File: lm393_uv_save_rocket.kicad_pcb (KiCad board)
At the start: 2 copper layers, 35 x 74 mm, 14 parts, among them J1 BAT 9V, J2 IGNITER, M3 M3, Q1 TIP122, U1 LM7805, U2 LM393

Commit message: Ajuste trilhas placa
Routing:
- net Net-(J2-Pin_1): track 35.3 -> 29.6 mm
- net Net-(D2-K): track 28.9 -> 34.1 mm
- net Net-(D2-A): track 27.0 -> 27.7 mm
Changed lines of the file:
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@@
+	)
+	(segment
+		(start 109 115.5)
+		(end 109 120.54)
+		(width 1.25)
+		(layer "B.Cu")
+		(net 2)
+	)
+	(segment
+		(start 110.747256 113.752744)
+		(end 109 115.5)
+		(width 1.25)
+		(layer "B.Cu")
+		(net 2)
 	)
 	(segment
@@
 	)
 	(segment
+		(start 109 120.54)
+		(end 110.75 120.54)
+		(width 1.25)
+		(layer "B.Cu")
+		(net 2)
+	)
+	(segment
 		(start 105.25 120.54)
-		(end 110.75 120.54)
+		(end 109 120.54)
 		(width 1.25)
 		(layer "B.Cu")
@@
 	(segment
 		(start 110.747256 109.77)
-		(end 110.747256 120.537256)
+		(end 110.747256 113.752744)
 		(width 1.25)
 		(layer "B.Cu")
@@
 	)
 	(segment
-		(start 108.705 128.25)
-		(end 105.25 128.25)
-		(width 1.25)
-		(layer "B.Cu")
-		(net 3)
-	)
-	(segment
-		(start 101.5 124.5)
-		(end 101.5 113.75)
+		(start 98.25 122.5)
+		(end 98.25 114)
 		(width 1.25)
 		(layer "B.Cu")
@@
 	)
 	(segment
+		(start 108.207256 111.457256)
+		(end 108.207256 109.77)
+		(width 1.25)
+		(layer "B.Cu")
+		(net 3)
+	)
+	(segment
+		(start 104 128.25)
+		(end 98.25 122.5)
+		(width 1.25)
+		(layer "B.Cu")
+		(net 3)
+	)
+	(segment
+		(start 108.705 128.25)
+		(end 104 128.25)
+		(width 1.25)
+		(layer "B.Cu")
+		(net 3)
+	)
+	(segment
+		(start 99.5 112.75)
+		(end 107 112.75)
+		(width 1.25)
+		(layer "B.Cu")
+		(net 3)
+	)
+	(segment
+		(start 98.25 114)
+		(end 99.5 112.75)
+		(width 1.25)
+		(layer "B.Cu")
+		(net 3)
+	)
+	(segment
 		(start 107 112.75)
 		(end 108.25 111.5)
@@
 	)
 	(segment
-		(start 105.25 128.25)
-		(end 101.5 124.5)
-		(width 1.25)
-		(layer "B.Cu")
-		(net 3)
-	)
-	(segment
-		(start 102.5 112.75)
-		(end 107 112.75)
-		(width 1.25)
-		(layer "B.Cu")
-		(net 3)
-	)
-	(segment
-		(start 108.207256 111.457256)
-		(end 108.207256 109.77)
-		(width 1.25)
-		(layer "B.Cu")
-		(net 3)
-	)
-	(segment
-		(start 101.5 113.75)
-		(end 102.5 112.75)
-		(width 1.25)
-		(layer "B.Cu")
-		(net 3)
-	)
-	(segment
 		(start 110.1637 95.5274)
 		(end 106.9137 95.5274)
@@
 	)
 	(segment
-		(start 89.75 128.25)
-		(end 89.75 126.25)
+		(start 89.529 98.856)
+		(end 89.529 128.044)
 		(width 1.25)
 		(layer "B.Cu")
@@
 	)
 	(segment
-		(start 96.75 119.25)
-		(end 96.75 108.5)
+		(start 89.615 98.77)
+		(end 89.529 98.856)
 		(width 1.25)
 		(layer "B.Cu")
@@
 	)
 	(segment
-		(start 89.75 126.25)
-		(end 96.75 119.25)
-		(width 1.25)
-		(layer "B.Cu")
-		(net 5)
-	)
-	(segment
-		(start 96.75 108.5)
-		(end 89.615 101.365)
-		(width 1.25)
-		(layer "B.Cu")
-		(net 5)
-	)
-	(segment
-		(start 89.615 101.365)
-		(end 89.615 98.77)
-		(width 1.25)
-		(layer "B.Cu")
+		(start 89.529 128.044)
+		(end 89.735 128.25)
+		(width 1.25)
+		(layer "B.Cu")

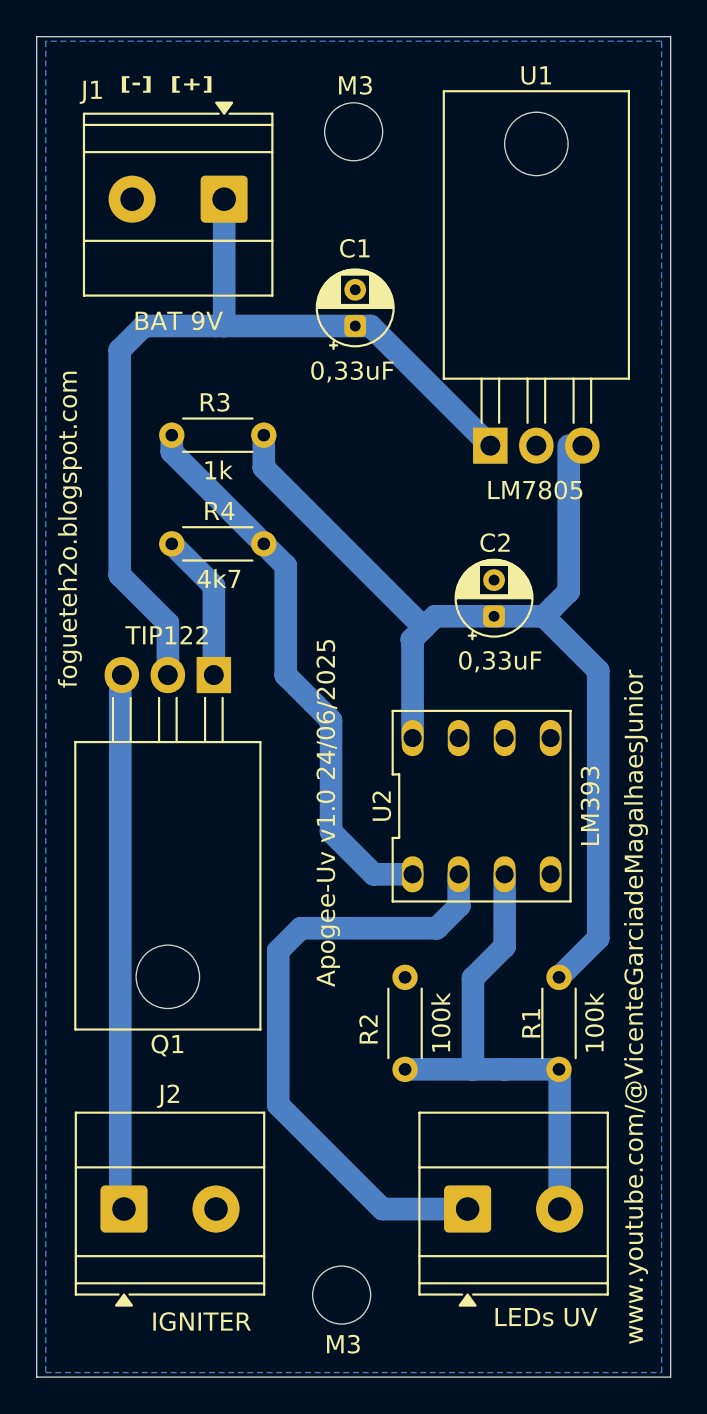
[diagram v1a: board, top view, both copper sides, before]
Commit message: Novo led que informa posição correta dos led UV, e funcionamento do circuito
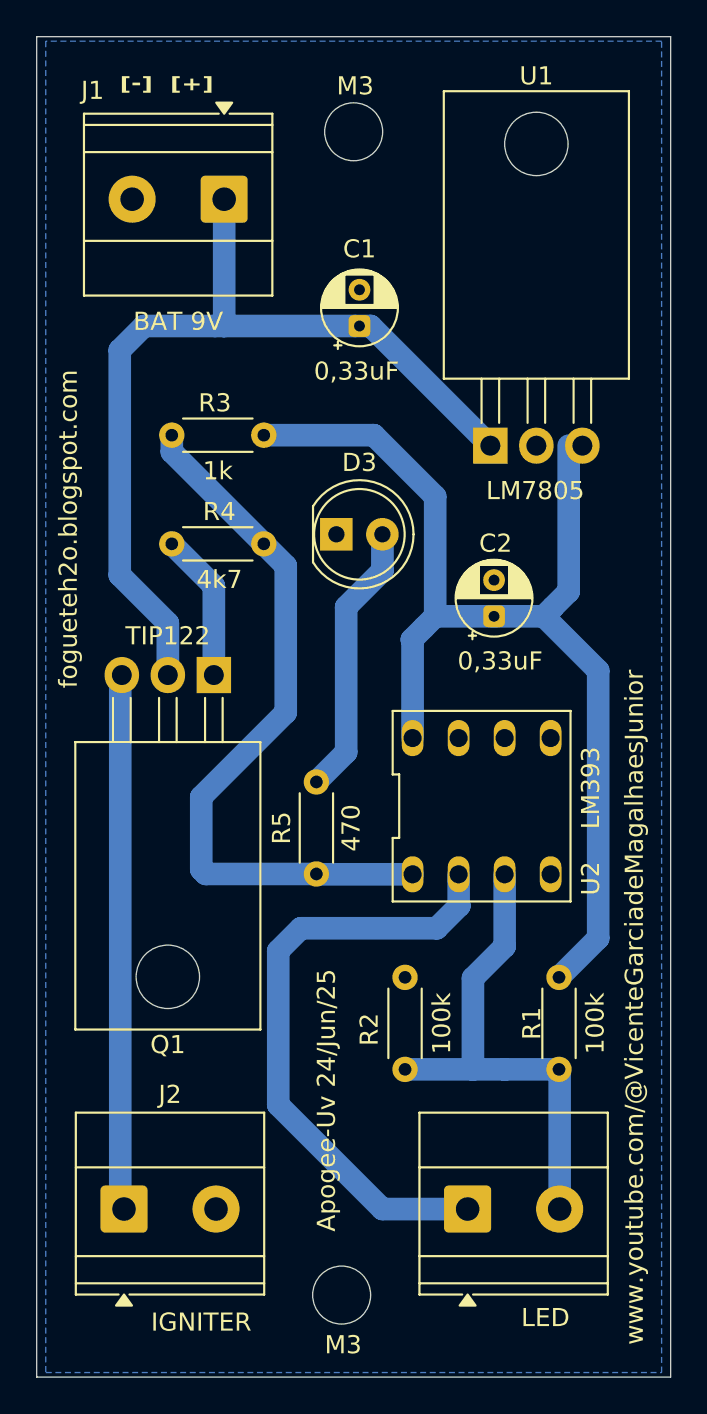
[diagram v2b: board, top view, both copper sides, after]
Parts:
- added D3: LED, LED_THT:LED_D5.0mm, F.Cu at (101.5, 91.0)
- added R5: 470, Resistor_THT:R_Axial_DIN0204_L3.6mm_D1.6mm_P5.08mm_Horizontal, F.Cu at (100.4, 109.8)
- D2: value LEDs UV -> LED
- moved C1 0.23 mm to (102.7, 79.5)
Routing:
- net Net-(D3-A): track 0.00 -> 15.2 mm
- net Net-(R3-Pad2): track 31.0 -> 40.3 mm
- net /VCC: track 59.6 -> 62.8 mm
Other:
- board text added: "Apogee-Uv 24/Jun/25"
- board text removed: "Apogee-Uv v1.0 24/06/2025"

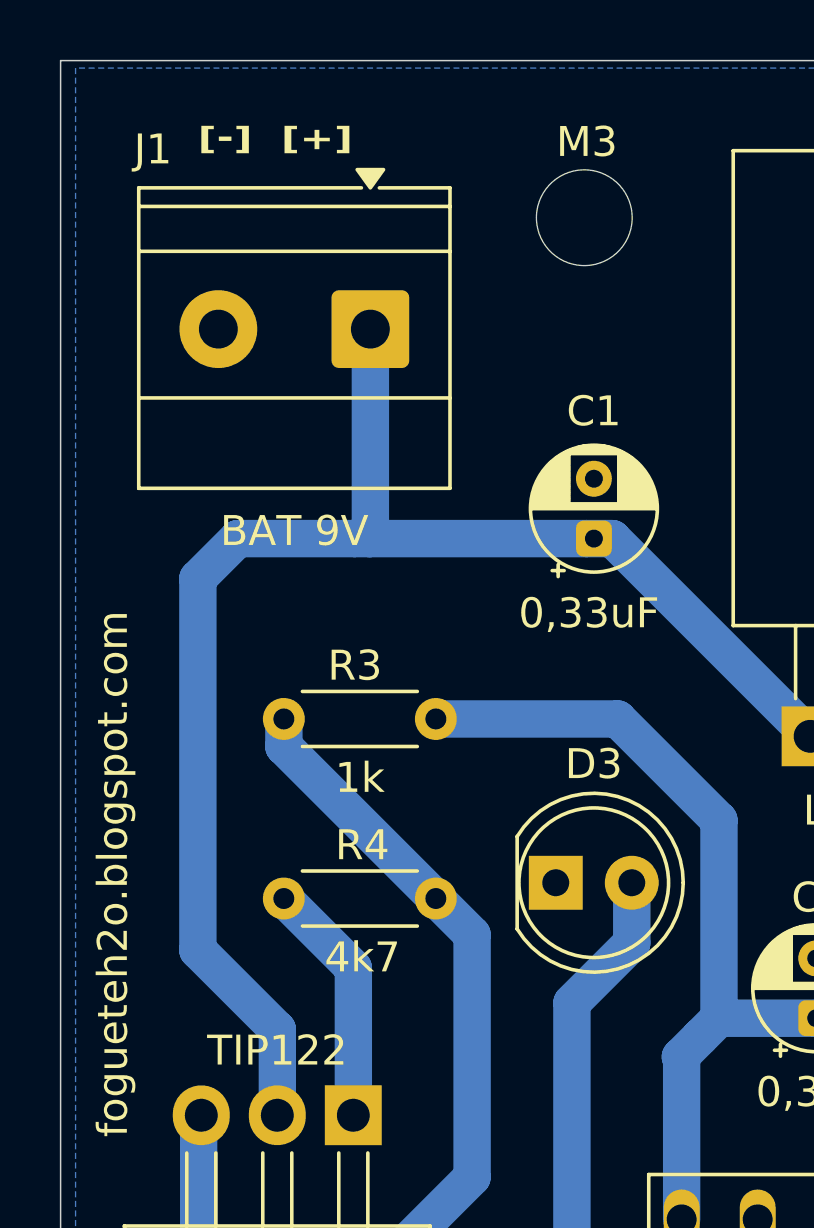
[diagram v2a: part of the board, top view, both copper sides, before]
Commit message: Alteração do tipo do conector da bat 9v
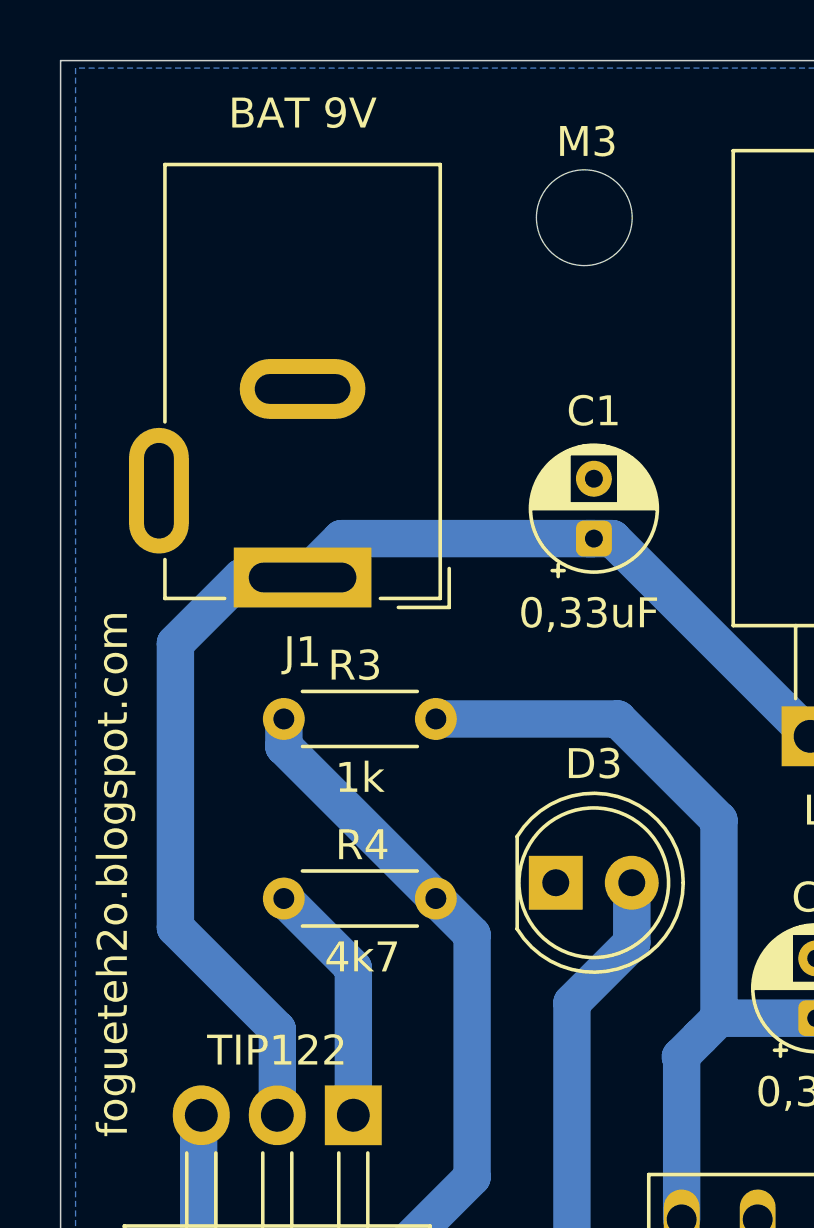
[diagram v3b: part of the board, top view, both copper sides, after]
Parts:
- J1: footprint TerminalBlock_Phoenix:TerminalBlock_Phoenix_MKDS-1,5-2-5.08_1x02_P5.08mm_Horizontal -> Connector_BarrelJack:BarrelJack_GCT_DCJ200-10-A_Horizontal
- moved J1 8.60 mm to (93.0, 80.8)
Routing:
- net Net-(J1-Pin_1): track 49.8 -> 42.8 mm
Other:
- board text removed: "[-] [+]"

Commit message: jumper de segurança
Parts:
- added J3: IGNITER, TerminalBlock_Phoenix:TerminalBlock_Phoenix_MKDS-1,5-2-5.08_1x02_P5.08mm_Horizontal, F.Cu at (89.7, 128.2)
- added JP1: Jumper_2_Bridged, TestPoint:TestPoint_Bridge_Pitch5.08mm_Drill0.7mm, F.Cu at (99.7, 115.5)
- J2: value IGNITER -> JUMP; footprint TerminalBlock_Phoenix:TerminalBlock_Phoenix_MKDS-1,5-2-5.08_1x02_P5.08mm_Horizontal -> Button_Switch_THT:SW_DIP_SPSTx01_Slide_6.7x4.1mm_W7.62mm_P2.54mm_LowProfile
- moved J2 14.3 mm to (102.0, 120.9), turned to -90 degrees
- moved R2 2.75 mm to (108.0, 115.5)
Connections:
- J2 pad 2: /GND -> Net-(J2-Pin_2)
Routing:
- net Net-(J2-Pin_2): track 0.00 -> 18.3 mm
- net Net-(D2-K): track 34.1 -> 27.7 mm
- net Net-(J2-Pin_1): track 29.6 -> 35.4 mm
- net Net-(D2-A): track 27.7 -> 24.2 mm
